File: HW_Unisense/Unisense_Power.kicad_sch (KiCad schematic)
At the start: 19 parts, among them Q10 IRLML6402TRPBF, Q8 IRLML6402TRPBF, Q9 IRLML6402TRPBF, U3 LD1117S33TR, U8 MCP73831T-2ATI/OT, U9 MAX17048G+T10

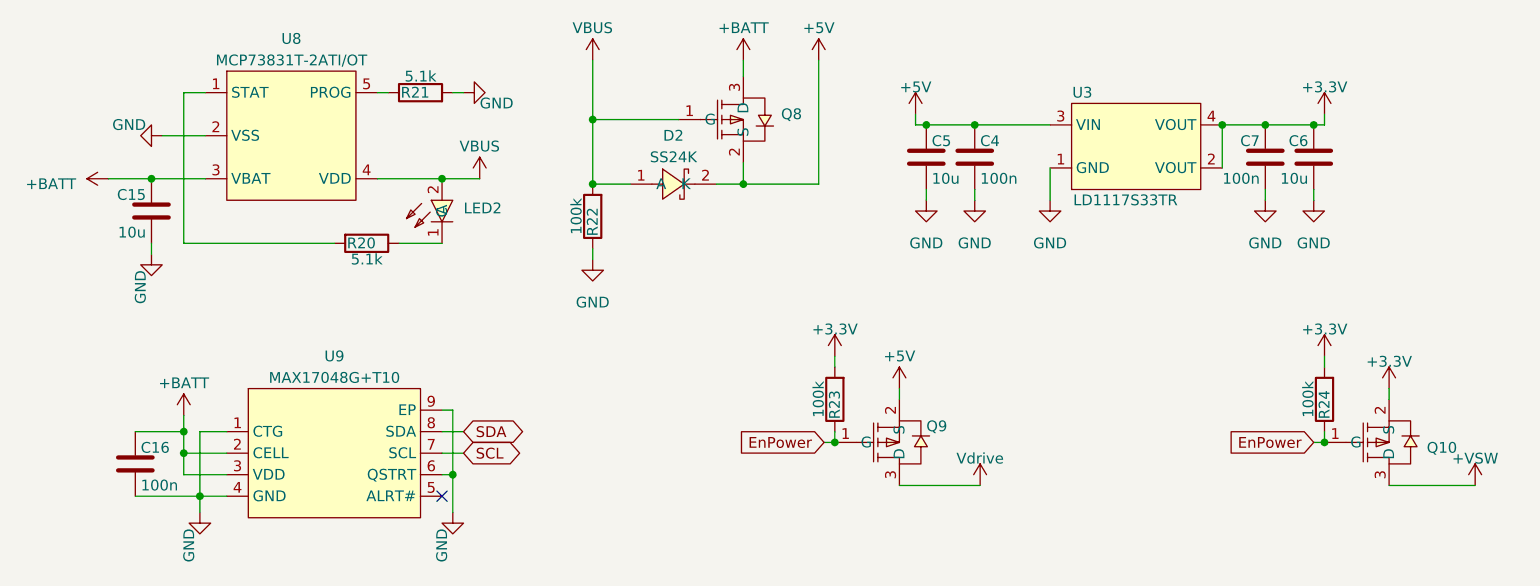
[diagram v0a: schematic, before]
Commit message: change power net names, as V8 handles them like a champ
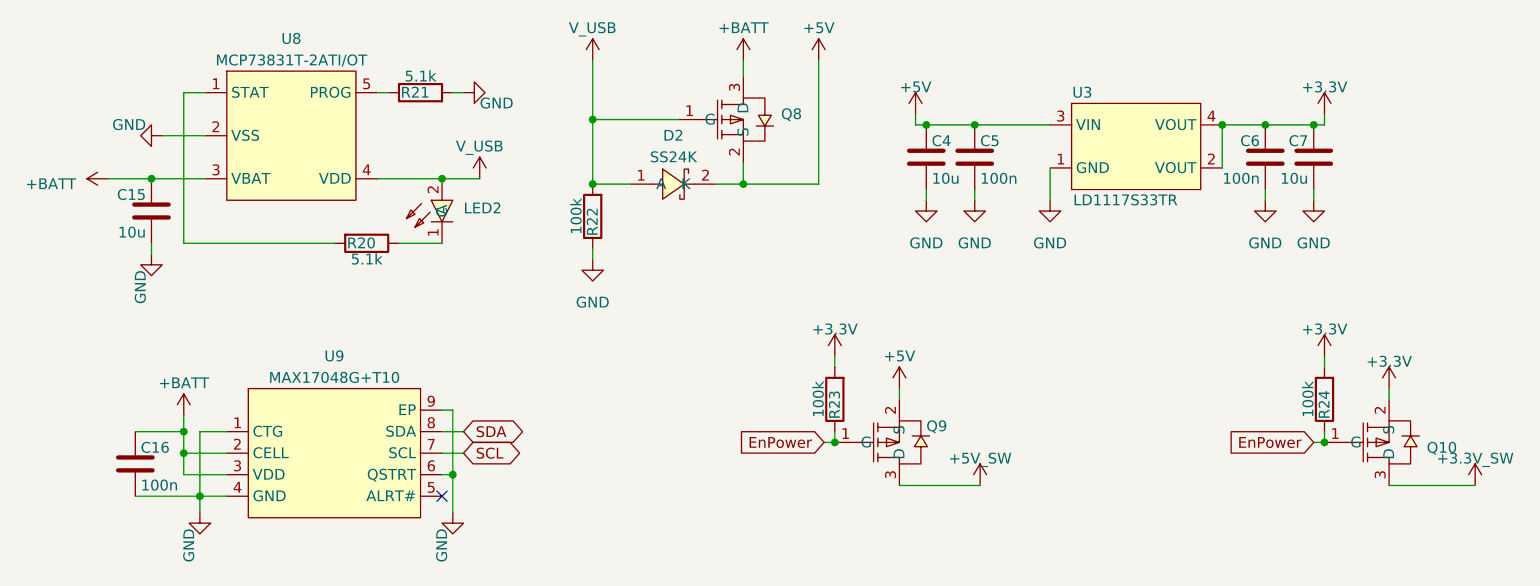
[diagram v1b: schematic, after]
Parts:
- renumbered C5 to C4, C4 to C5, C7 to C6, C6 to C7
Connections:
- net +VSW renamed +3.3V_SW
- net VBUS renamed V_USB
- net Vdrive renamed +5V_SW
